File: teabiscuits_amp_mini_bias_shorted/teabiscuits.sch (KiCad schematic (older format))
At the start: 18 parts, among them J1 Conn_Coaxial, J2 Conn_Coaxial, J3 Conn_01x03_Male, J4 Conn_Coaxial, U2 LMP7721, U3 OP07

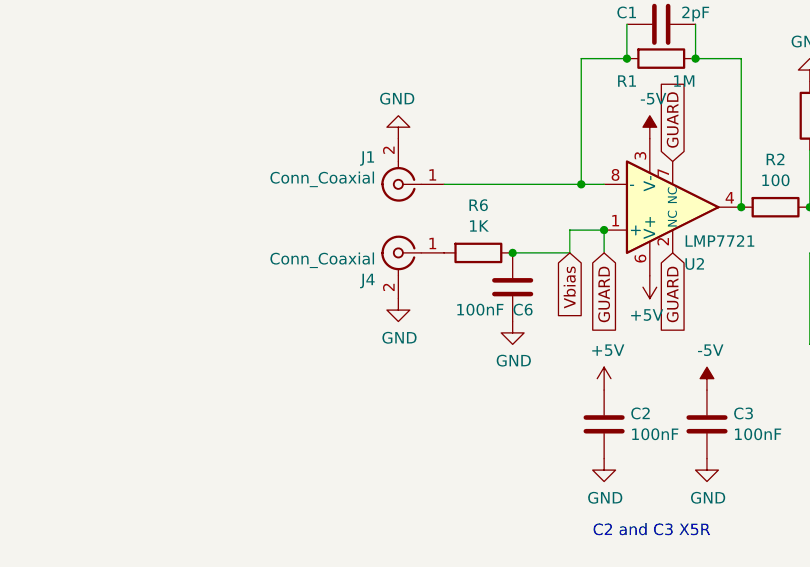
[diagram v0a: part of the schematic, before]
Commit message: Some strangeness
I'm not exactly sure why these are changes, but ... I'm checking them
in all the same...
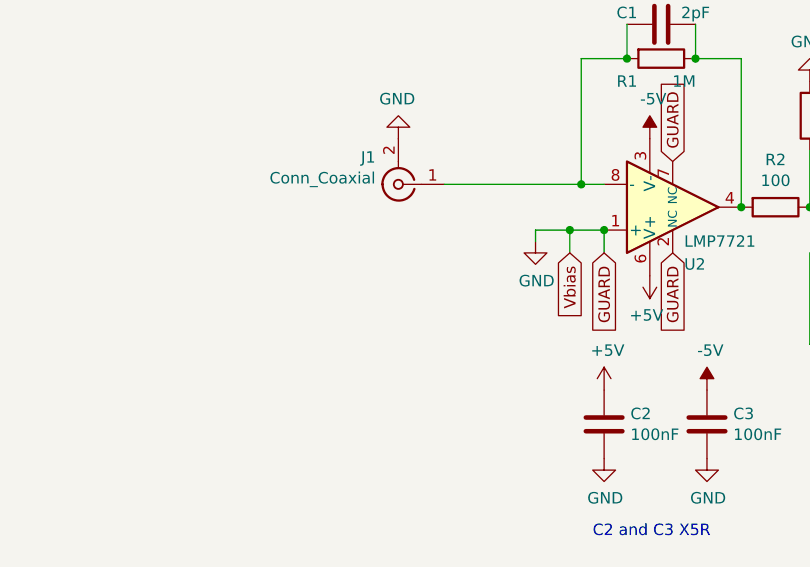
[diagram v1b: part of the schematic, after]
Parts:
- removed C6: 100nF, Capacitor_SMD:C_0805_2012Metric, symbol Device:C
- removed J4: Conn_Coaxial, Connector_Coaxial:MMCX_Molex_73415-0961_Horizontal_1.0mm-PCB, symbol Connector:Conn_Coaxial
- removed R6: 1K, Resistor_SMD:R_0805_2012Metric, symbol Device:R
- J3: footprint Connector_PinSocket_2.54mm:PinSocket_1x03_P2.54mm_Horizontal -> Connector_PinSocket_1.27mm:PinSocket_1x03_P1.27mm_Vertical
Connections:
- net GUARD is gone; now on net GND: R4.1, U2.1 (+), U2.2 (NC), U2.7 (NC)
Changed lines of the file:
@@
 F 0 "J3" H 1022 882 50  0000 R CNN
 F 1 "Conn_01x03_Male" H 1022 973 50  0000 R CNN
-F 2 "Connector_PinSocket_2.54mm:PinSocket_1x03_P2.54mm_Horizontal" H 1050 950 50  0001 C CNN
+F 2 "Connector_PinSocket_1.27mm:PinSocket_1x03_P1.27mm_Vertical" H 1050 950 50  0001 C CNN
 F 3 "~" H 1050 950 50  0001 C CNN
 	1    1050 950
@@
 	1    0    0    -1
 $EndComp
-$Comp
-L Connector:Conn_Coaxial J4
-U 1 1 5EFB71A9
-P 5350 3300
-F 0 "J4" H 5450 3182 50  0000 L CNN
-F 1 "Conn_Coaxial" H 5450 3273 50  0000 L CNN
-F 2 "Connector_Coaxial:MMCX_Molex_73415-0961_Horizontal_1.0mm-PCB" H 5350 3300 50  0001 C CNN
-F 3 " ~" H 5350 3300 50  0001 C CNN
-	1    5350 3300
-	-1   0    0    -1
-$EndComp
-$Comp
-L power:GND #PWR0121
-U 1 1 5EFBB96C
-P 5350 3500
-F 0 "#PWR0121" H 5350 3250 50  0001 C CNN
-F 1 "GND" H 5355 3327 50  0000 C CNN
-F 2 "" H 5350 3500 50  0001 C CNN
-F 3 "" H 5350 3500 50  0001 C CNN
-	1    5350 3500
-	1    0    0    -1
-$EndComp
 Text GLabel 6250 3300 3    50   Input ~ 0
 GUARD
@@
 	7150 3700 7150 3300
 Text GLabel 7750 4000 3    50   Input ~ 0
-Vbias
-Text GLabel 6100 3300 3    50   Input ~ 0
 Vbias
 $Comp
@@
 Wire Wire Line
 	7150 2850 7150 3100
-$Comp
-L Device:R R6
-U 1 1 5F28EE92
-P 5700 3300
-F 0 "R6" V 5493 3300 50  0000 C CNN
-F 1 "1K" V 5584 3300 50  0000 C CNN
-F 2 "Resistor_SMD:R_0805_2012Metric" V 5630 3300 50  0001 C CNN
-F 3 "~" H 5700 3300 50  0001 C CNN
-	1    5700 3300
-	0    1    1    0
-$EndComp
-Wire Wire Line
-	5850 3300 6100 3300
 Wire Wire Line
 	6250 3200 6100 3200
@@
 Connection ~ 6250 3200
 $Comp
-L Device:C C6
-U 1 1 5F28FF65
-P 5850 3450
-F 0 "C6" H 5850 3350 50  0000 L CNN
-F 1 "100nF" H 5600 3350 50  0000 L CNN
-F 2 "Capacitor_SMD:C_0805_2012Metric" H 5888 3300 50  0001 C CNN
-F 3 "~" H 5850 3450 50  0001 C CNN
-	1    5850 3450
+L power:GND #PWR02
+U 1 1 5F290867
+P 5950 3250
+F 0 "#PWR02" H 5950 3000 50  0001 C CNN
+F 1 "GND" H 5955 3077 50  0000 C CNN
+F 2 "" H 5950 3250 50  0001 C CNN
+F 3 "" H 5950 3250 50  0001 C CNN
+	1    5950 3250
 	1    0    0    -1
 $EndComp
-Connection ~ 5850 3300
-$Comp
-L power:GND #PWR02
-U 1 1 5F290867
-P 5850 3600
-F 0 "#PWR02" H 5850 3350 50  0001 C CNN
-F 1 "GND" H 5855 3427 50  0000 C CNN
-F 2 "" H 5850 3600 50  0001 C CNN
-F 3 "" H 5850 3600 50  0001 C CNN
-	1    5850 3600
-	1    0    0    -1
-$EndComp
+Text GLabel 6100 3300 3    50   Input ~ 0
+Vbias
+Wire Wire Line
+	6100 3200 5950 3200
+Wire Wire Line
+	5950 3200 5950 3250
+Connection ~ 6100 3200
 $EndSCHEMATC
